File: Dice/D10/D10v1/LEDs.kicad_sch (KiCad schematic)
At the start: 13 parts

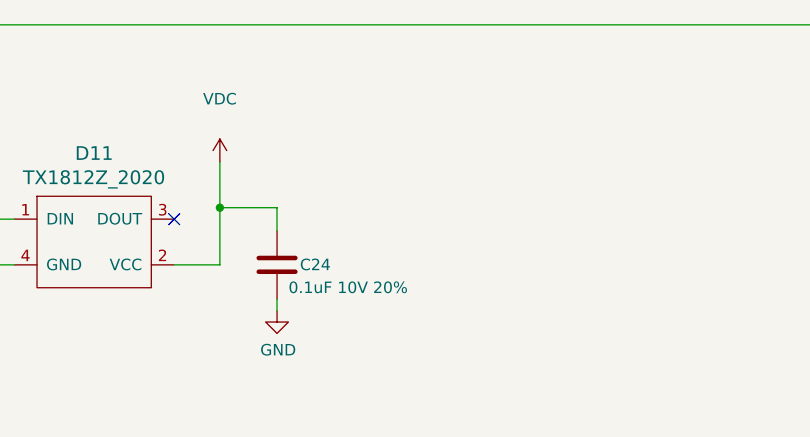
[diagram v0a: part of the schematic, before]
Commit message: Added D10, D00 and D8, D20V12 updates
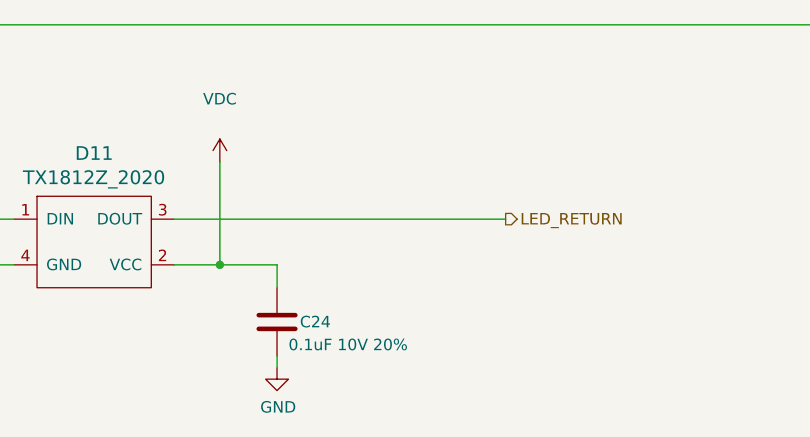
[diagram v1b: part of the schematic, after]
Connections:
- net LED_RETURN: now reaches D11.3 (DOUT)
- no-connect marks 1 -> 0
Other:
- moved on the sheet: C24
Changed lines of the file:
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@@
   (junction (at 25.4 46.99) (diameter 0) (color 0 0 0 0)
   )
-  (junction (at 144.78 90.17) (diameter 0) (color 0 0 0 0)
+  (junction (at 144.78 96.52) (diameter 0) (color 0 0 0 0)
   )
   (junction (at 266.7 52.07) (diameter 0) (color 0 0 0 0)
   )
-  (no_connect (at 139.7 91.44))
-  (wire (pts (xy 144.78 90.17) (xy 151.13 90.17))
+  (wire (pts (xy 144.78 96.52) (xy 151.13 96.52))
     (stroke (width 0) (type default) (color 0 0 0 0))
   )
@@
     (stroke (width 0) (type default) (color 0 0 0 0))
   )
-  (wire (pts (xy 151.13 92.71) (xy 151.13 90.17))
+  (wire (pts (xy 151.13 99.06) (xy 151.13 96.52))
     (stroke (width 0) (type default) (color 0 0 0 0))
   )
@@
     (stroke (width 0) (type default) (color 0 0 0 0))
   )
-  (wire (pts (xy 151.13 100.33) (xy 151.13 101.6))
+  (wire (pts (xy 151.13 106.68) (xy 151.13 107.95))
     (stroke (width 0) (type default) (color 0 0 0 0))
   )
@@
     (stroke (width 0) (type default) (color 0 0 0 0))
   )
+  (wire (pts (xy 139.7 91.44) (xy 176.53 91.44))
+    (stroke (width 0) (type default) (color 0 0 0 0))
+  )
   (wire (pts (xy 105.41 46.99) (xy 121.92 46.99))
     (stroke (width 0) (type default) (color 0 0 0 0))
@@
     (stroke (width 0) (type default) (color 0 0 0 0))
   )
-  (wire (pts (xy 144.78 90.17) (xy 144.78 96.52))
-    (stroke (width 0) (type default) (color 0 0 0 0))
-  )
   (wire (pts (xy 173.99 40.64) (xy 173.99 52.07))
     (stroke (width 0) (type default) (color 0 0 0 0))
@@
     (stroke (width 0) (type default) (color 0 0 0 0))
   )
-  (wire (pts (xy 144.78 85.09) (xy 144.78 90.17))
+  (wire (pts (xy 144.78 85.09) (xy 144.78 96.52))
     (stroke (width 0) (type default) (color 0 0 0 0))
   )
@@
     (effects (font (size 1.27 1.27)) (justify right))
   )
+  (hierarchical_label "LED_RETURN" (shape output) (at 176.53 91.44 0)
+    (effects (font (size 1.27 1.27)) (justify left))
+  )
   (hierarchical_label "VLED" (shape input) (at 24.13 30.48 180)
     (effects (font (size 1.27 1.27)) (justify right))
@@
     (pin "1")
   )
-  (symbol (lib_id "Device:C") (at 151.13 96.52 0) (unit 1)
-    (in_bom yes) (on_board yes)
-    (property "Reference" "C24" (id 0) (at 153.67 96.52 0)
+  (symbol (lib_id "Device:C") (at 151.13 102.87 0) (unit 1)
+    (in_bom yes) (on_board yes)
+    (property "Reference" "C24" (id 0) (at 153.67 102.87 0)
       (effects (font (size 1.27 1.27)) (justify left))
     )
-    (property "Value" "0.1uF 10V 20%" (id 1) (at 152.4 99.06 0)
+    (property "Value" "0.1uF 10V 20%" (id 1) (at 152.4 105.41 0)
       (effects (font (size 1.27 1.27)) (justify left))
     )
-    (property "Footprint" "Capacitor_SMD:C_0402_1005Metric" (id 2) (at 152.0952 100.33 0)
-      (effects (font (size 1.27 1.27)) hide)
-    )
-    (property "Datasheet" "~" (id 3) (at 151.13 96.52 0)
-      (effects (font (size 1.27 1.27)) hide)
-    )
-    (property "Generic OK" "YES" (id 4) (at 151.13 96.52 0)
-      (effects (font (size 1.27 1.27)) hide)
-    )
-    (property "Pixels Part Number" "SMD-C005" (id 5) (at 151.13 96.52 0)
-      (effects (font (size 1.27 1.27)) hide)
-    )
-    (property "Manufacturer" "Murata" (id 6) (at 151.13 96.52 0)
-      (effects (font (size 1.27 1.27)) hide)
-    )
-    (property "Manufacturer Part Number" "GRM155R61H104KE19D" (id 7) (at 151.13 96.52 0)
+    (property "Footprint" "Capacitor_SMD:C_0402_1005Metric" (id 2) (at 152.0952 106.68 0)
+      (effects (font (size 1.27 1.27)) hide)
+    )
+    (property "Datasheet" "~" (id 3) (at 151.13 102.87 0)
+      (effects (font (size 1.27 1.27)) hide)
+    )
+    (property "Generic OK" "YES" (id 4) (at 151.13 102.87 0)
+      (effects (font (size 1.27 1.27)) hide)
+    )
+    (property "Pixels Part Number" "SMD-C005" (id 5) (at 151.13 102.87 0)
+      (effects (font (size 1.27 1.27)) hide)
+    )
+    (property "Manufacturer" "Murata" (id 6) (at 151.13 102.87 0)
+      (effects (font (size 1.27 1.27)) hide)
+    )
+    (property "Manufacturer Part Number" "GRM155R61H104KE19D" (id 7) (at 151.13 102.87 0)
       (effects (font (size 1.27 1.27)) hide)
     )
@@
     (pin "2")
   )
-  (symbol (lib_id "power:GND") (at 151.13 101.6 0) (unit 1)
-    (in_bom yes) (on_board yes)
-    (property "Reference" "#PWR0141" (id 0) (at 151.13 107.95 0)
-      (effects (font (size 1.27 1.27)) hide)
-    )
-    (property "Value" "GND" (id 1) (at 151.257 105.9942 0))
-    (property "Footprint" "" (id 2) (at 151.13 101.6 0)
-      (effects (font (size 1.27 1.27)) hide)
-    )
-    (property "Datasheet" "" (id 3) (at 151.13 101.6 0)
-      (effects (font (size 1.27 1.27)) hide)
-    )
+  (symbol (lib_id "power:GND") (at 151.13 107.95 0) (unit 1)
+    (in_bom yes) (on_board yes)
+    (property "Reference" "#PWR0141" (id 0) (at 151.13 114.3 0)
+      (effects (font (size 1.27 1.27)) hide)
+    )
+    (property "Value" "GND" (id 1) (at 151.257 112.3442 0))
+    (property "Footprint" "" (id 2) (at 151.13 107.95 0)
+      (effects (font (size 1.27 1.27)) hide)
+    )
+    (property "Datasheet" "" (id 3) (at 151.13 107.95 0)
+      (effects (font (size 1.27 1.27)) hide)
+    )

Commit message: Updating D8 and D10 boards, new antenna, etc...
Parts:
- W22: Generic OK (none) -> N/A
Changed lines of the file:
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@@
     )
     (property "Datasheet" "" (id 3) (at 30.48 45.72 0))
+    (property "Generic OK" "N/A" (id 4) (at 25.4 45.72 0)
+      (effects (font (size 1.27 1.27)) hide)
+    )
     (pin "1")
   )
